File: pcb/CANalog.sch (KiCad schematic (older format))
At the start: 97 parts, among them J1 PWR, J2 USB_B_Micro, J3 SPI3, J4 I2C2, J5 STM_PROG, J6 ESP_PROG, J7 AOUT, J8 CAN, Q1 DMP3099L-7, Q2 MMBT2222A, Q3 DMP3099L-7, SW1 RESET, SW2 ESP_PROG, U1 BL9342, U2 RS321BXF, U3 STM32F302C8T6, U4 ESP-12F, U5 MIC5504-3.3YM5, U6 OPA330xxDBV, U7 SN65HVD230, U8 74AHC1G66, Y1 16MHz

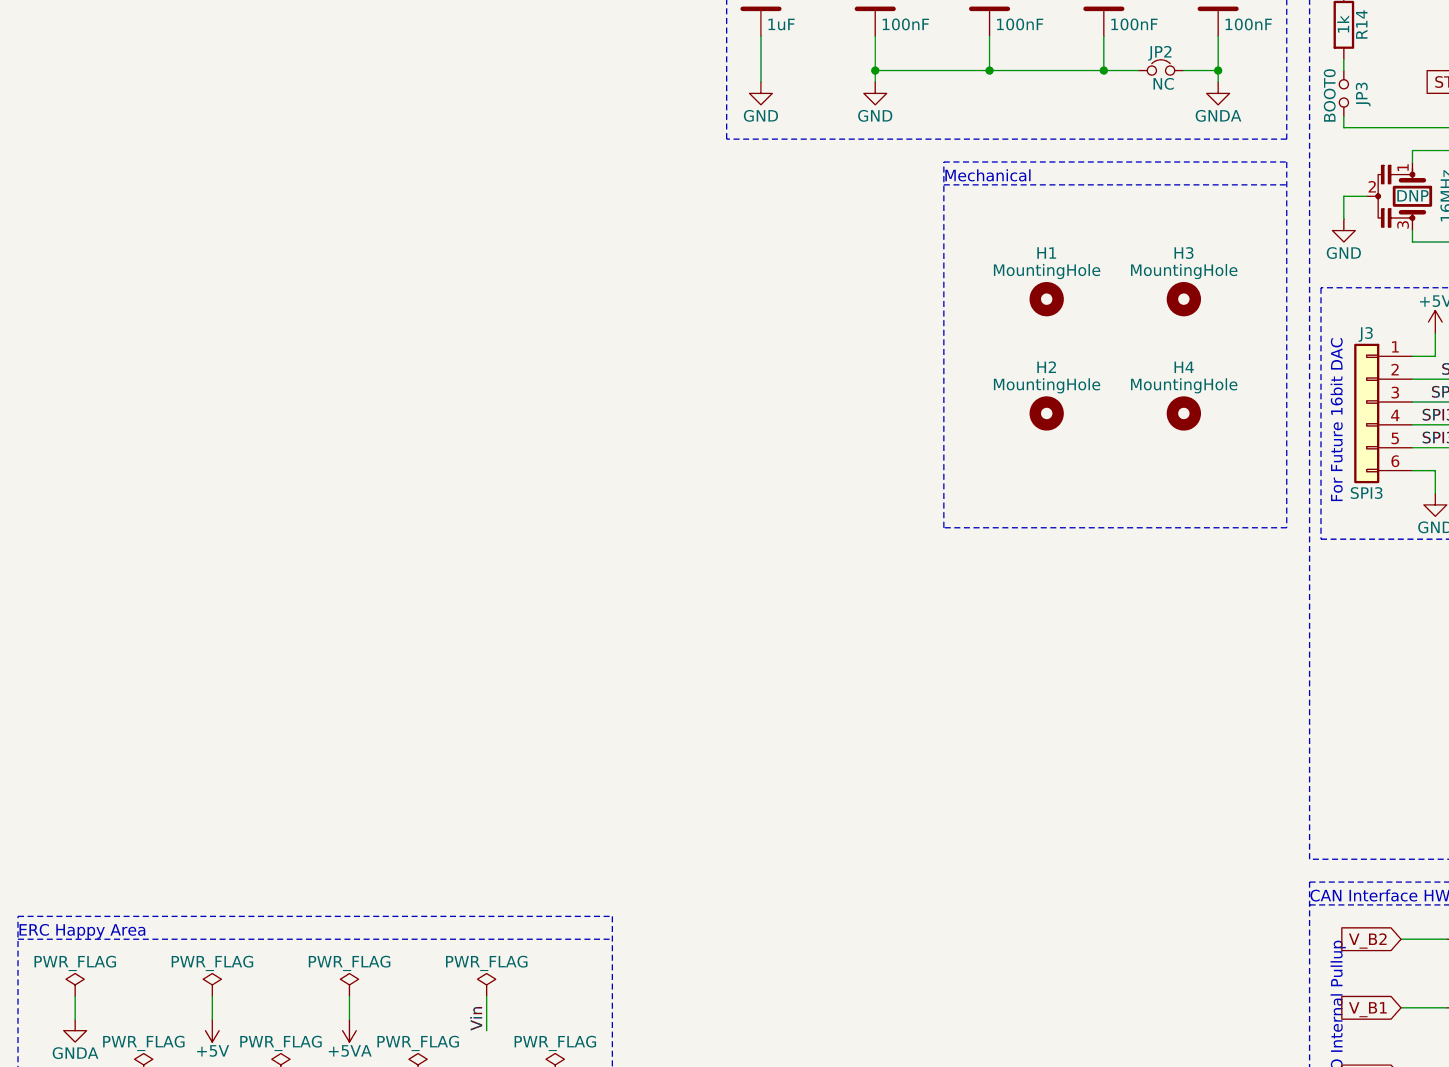
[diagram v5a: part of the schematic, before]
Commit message: usb fuse part number change to instock
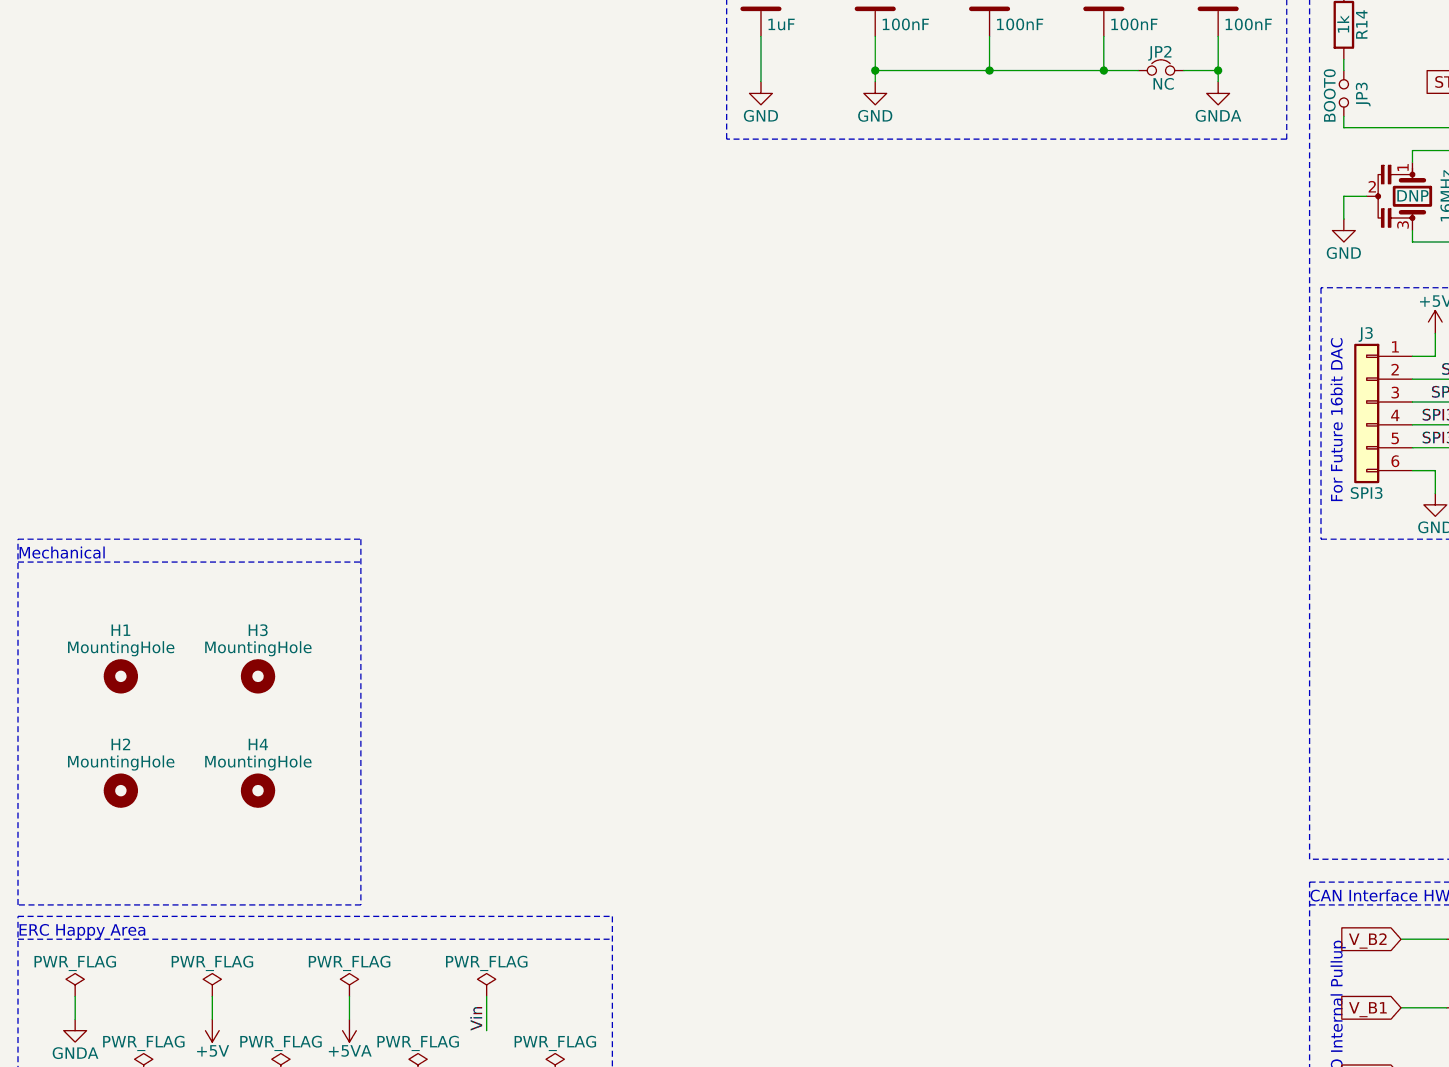
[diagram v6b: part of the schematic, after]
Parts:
- F1: MPN MF-FSMF050X-2 -> BSMD0603-050-6V; Manufacture Bourns -> BHFUSE; SPN C210357 -> C883095; Supplier Link https://lcsc.com/product-detail/Surface-Mount-Fuses_BOURNS_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 -> https://lcsc.com/product-detail/PTC-Resettable-Fuses_BHFUSE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
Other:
- moved on the sheet: H1, H2, H3, H4
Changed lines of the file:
@@
 L Mechanical:MountingHole H1
 U 1 1 61BCE530
-P 5050 6650
-F 0 "H1" H 5050 6850 50  0000 C CNN
-F 1 "MountingHole" H 5050 6775 50  0000 C CNN
-F 2 "MountingHole:MountingHole_2.7mm_M2.5" H 5050 6650 50  0001 C CNN
-F 3 "~" H 5050 6650 50  0001 C CNN
-	1    5050 6650
+P 1000 8300
+F 0 "H1" H 1000 8500 50  0000 C CNN
+F 1 "MountingHole" H 1000 8425 50  0000 C CNN
+F 2 "MountingHole:MountingHole_2.7mm_M2.5" H 1000 8300 50  0001 C CNN
+F 3 "~" H 1000 8300 50  0001 C CNN
+	1    1000 8300
 	1    0    0    -1
 $EndComp
@@
 L Mechanical:MountingHole H3
 U 1 1 61BCEAAF
-P 5650 6650
-F 0 "H3" H 5650 6850 50  0000 C CNN
-F 1 "MountingHole" H 5650 6775 50  0000 C CNN
-F 2 "MountingHole:MountingHole_2.7mm_M2.5" H 5650 6650 50  0001 C CNN
-F 3 "~" H 5650 6650 50  0001 C CNN
-	1    5650 6650
+P 1600 8300
+F 0 "H3" H 1600 8500 50  0000 C CNN
+F 1 "MountingHole" H 1600 8425 50  0000 C CNN
+F 2 "MountingHole:MountingHole_2.7mm_M2.5" H 1600 8300 50  0001 C CNN
+F 3 "~" H 1600 8300 50  0001 C CNN
+	1    1600 8300
 	1    0    0    -1
 $EndComp
@@
 L Mechanical:MountingHole H4
 U 1 1 61BCF017
-P 5650 7150
-F 0 "H4" H 5650 7350 50  0000 C CNN
-F 1 "MountingHole" H 5650 7275 50  0000 C CNN
-F 2 "MountingHole:MountingHole_2.7mm_M2.5" H 5650 7150 50  0001 C CNN
-F 3 "~" H 5650 7150 50  0001 C CNN
-	1    5650 7150
+P 1600 8800
+F 0 "H4" H 1600 9000 50  0000 C CNN
+F 1 "MountingHole" H 1600 8925 50  0000 C CNN
+F 2 "MountingHole:MountingHole_2.7mm_M2.5" H 1600 8800 50  0001 C CNN
+F 3 "~" H 1600 8800 50  0001 C CNN
+	1    1600 8800
 	1    0    0    -1
 $EndComp
@@
 L Mechanical:MountingHole H2
 U 1 1 61BCF67B
-P 5050 7150
-F 0 "H2" H 5050 7350 50  0000 C CNN
-F 1 "MountingHole" H 5050 7275 50  0000 C CNN
-F 2 "MountingHole:MountingHole_2.7mm_M2.5" H 5050 7150 50  0001 C CNN
-F 3 "~" H 5050 7150 50  0001 C CNN
-	1    5050 7150
+P 1000 8800
+F 0 "H2" H 1000 9000 50  0000 C CNN
+F 1 "MountingHole" H 1000 8925 50  0000 C CNN
+F 2 "MountingHole:MountingHole_2.7mm_M2.5" H 1000 8800 50  0001 C CNN
+F 3 "~" H 1000 8800 50  0001 C CNN
+	1    1000 8800
 	1    0    0    -1
 $EndComp
@@
 F 1 "500mA" V 1316 3050 50  0000 C CNN
 F 2 "Fuse:Fuse_0603_1608Metric_Castellated" H 1500 2850 50  0001 L CNN
-F 3 "~https://datasheet.lcsc.com/szlcsc/1806111858_BOURNS-MF-FSMF050X-2_C210357.pdf" H 1450 3050 50  0001 C CNN
-F 4 "MF-FSMF050X-2" H 1450 3050 50  0001 C CNN "MPN"
-F 5 "Bourns" H 1450 3050 50  0001 C CNN "Manufacture"
-F 6 "C210357" H 1450 3050 50  0001 C CNN "SPN"
+F 3 "https://datasheet.lcsc.com/szlcsc/2103231635_BHFUSE-BSMD0603-050-6V_C883095.pdf" H 1450 3050 50  0001 C CNN
+F 4 "BSMD0603-050-6V" H 1450 3050 50  0001 C CNN "MPN"
+F 5 " BHFUSE" H 1450 3050 50  0001 C CNN "Manufacture"
+F 6 "C883095" H 1450 3050 50  0001 C CNN "SPN"
 F 7 "LCSC" H 1450 3050 50  0001 C CNN "Supplier"
-F 8 "https://lcsc.com/product-detail/Surface-Mount-Fuses_BOURNS_MF-FSMF050X-2_BOURNS-MF-FSMF050X-2_C210357.html" H 1450 3050 50  0001 C CNN "Supplier Link"
+F 8 "https://lcsc.com/product-detail/PTC-Resettable-Fuses_BHFUSE-BSMD0603-050-6V_C883095.html" H 1450 3050 50  0001 C CNN "Supplier Link"
 	1    1450 3050
 	0    1    1    0
@@
 Text Notes 3900 3150 0    50   ~ 0
 Reset Circuitry
-Text Notes 4600 6150 0    50   ~ 0
+Text Notes 550  7800 0    50   ~ 0
 Mechanical
 Wire Notes Line
-	4600 6150 6100 6150
-Wire Notes Line
-	6100 7650 4600 7650
-Wire Notes Line
-	4600 7650 4600 6050
-Wire Notes Line
-	4600 6050 6100 6050
-Wire Notes Line
-	6100 6050 6100 7650
+	550  7800 2050 7800
+Wire Notes Line
+	2050 9300 550  9300
+Wire Notes Line
+	550  9300 550  7700
+Wire Notes Line
+	550  7700 2050 7700
+Wire Notes Line
+	2050 7700 2050 9300
 Text Notes 550  9450 0    50   ~ 0
 ERC Happy Area

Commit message: update ferrite with instock partnumber
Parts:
- FB1, FB2: MPN CBG160808U070T -> FCM1608KF-600T07; Manufacture FH(Guangdong Fenghua Advanced Tech) -> TAI-TECH; SPN C98494 -> C133931; Supplier Link https://lcsc.com/product-detail/Ferrite-Beads_FH-Guangdong-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 -> https://lcsc.com/product-detail/Ferrite-Beads_TAI-TECH-FCM1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
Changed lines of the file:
@@
 F 1 "FBS" V 12150 7350 50  0000 C CNN
 F 2 "Inductor_SMD:L_0603_1608Metric" V 11980 7350 50  0001 C CNN
-F 3 "https://datasheet.lcsc.com/szlcsc/2006221432_FH-Guangdong-Fenghua-Advanced-Tech-CBG160808U070T_C98494.pdf" H 12050 7350 50  0001 C CNN
-F 4 "CBG160808U070T" H 12050 7350 50  0001 C CNN "MPN"
-F 5 " FH(Guangdong Fenghua Advanced Tech)" H 12050 7350 50  0001 C CNN "Manufacture"
-F 6 "C98494" H 12050 7350 50  0001 C CNN "SPN"
+F 3 "https://datasheet.lcsc.com/szlcsc/2009171304_TAI-TECH-FCM1608KF-600T07_C133931.pdf" H 12050 7350 50  0001 C CNN
+F 4 "FCM1608KF-600T07" H 12050 7350 50  0001 C CNN "MPN"
+F 5 "TAI-TECH" H 12050 7350 50  0001 C CNN "Manufacture"
+F 6 "C133931" H 12050 7350 50  0001 C CNN "SPN"
 F 7 "LCSC" H 12050 7350 50  0001 C CNN "Supplier"
-F 8 "https://lcsc.com/product-detail/Ferrite-Beads_FH-Guangdong-Fenghua-Advanced-Tech-CBG160808U070T_C98494.html" H 12050 7350 50  0001 C CNN "Supplier Link"
+F 8 "https://lcsc.com/product-detail/Ferrite-Beads_TAI-TECH-FCM1608KF-600T07_C133931.html" H 12050 7350 50  0001 C CNN "Supplier Link"
 	1    12050 7350
 	0    -1   -1   0
@@
 F 1 "FBS" V 5650 5100 50  0000 C CNN
 F 2 "Inductor_SMD:L_0603_1608Metric" V 5480 5100 50  0001 C CNN
-F 3 "https://datasheet.lcsc.com/szlcsc/2006221432_FH-Guangdong-Fenghua-Advanced-Tech-CBG160808U070T_C98494.pdf" H 5550 5100 50  0001 C CNN
-F 4 "CBG160808U070T" H 5550 5100 50  0001 C CNN "MPN"
-F 5 " FH(Guangdong Fenghua Advanced Tech)" H 5550 5100 50  0001 C CNN "Manufacture"
-F 6 "C98494" H 5550 5100 50  0001 C CNN "SPN"
+F 3 "https://datasheet.lcsc.com/szlcsc/2009171304_TAI-TECH-FCM1608KF-600T07_C133931.pdf" H 5550 5100 50  0001 C CNN
+F 4 "FCM1608KF-600T07" H 5550 5100 50  0001 C CNN "MPN"
+F 5 "TAI-TECH" H 5550 5100 50  0001 C CNN "Manufacture"
+F 6 "C133931" H 5550 5100 50  0001 C CNN "SPN"
 F 7 "LCSC" H 5550 5100 50  0001 C CNN "Supplier"
-F 8 "https://lcsc.com/product-detail/Ferrite-Beads_FH-Guangdong-Fenghua-Advanced-Tech-CBG160808U070T_C98494.html" H 5550 5100 50  0001 C CNN "Supplier Link"
+F 8 "https://lcsc.com/product-detail/Ferrite-Beads_TAI-TECH-FCM1608KF-600T07_C133931.html" H 5550 5100 50  0001 C CNN "Supplier Link"
 	1    5550 5100
 	0    -1   -1   0

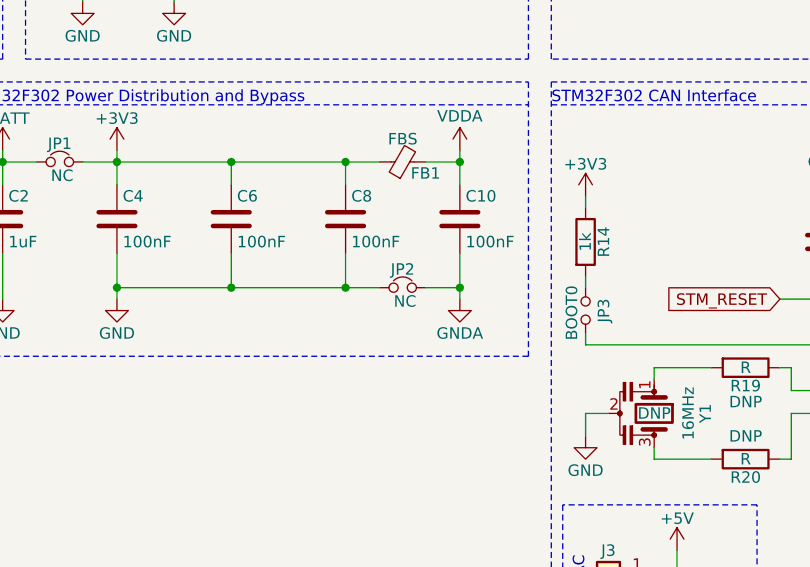
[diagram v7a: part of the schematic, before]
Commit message: replace agnd jumper to gnd with net tie
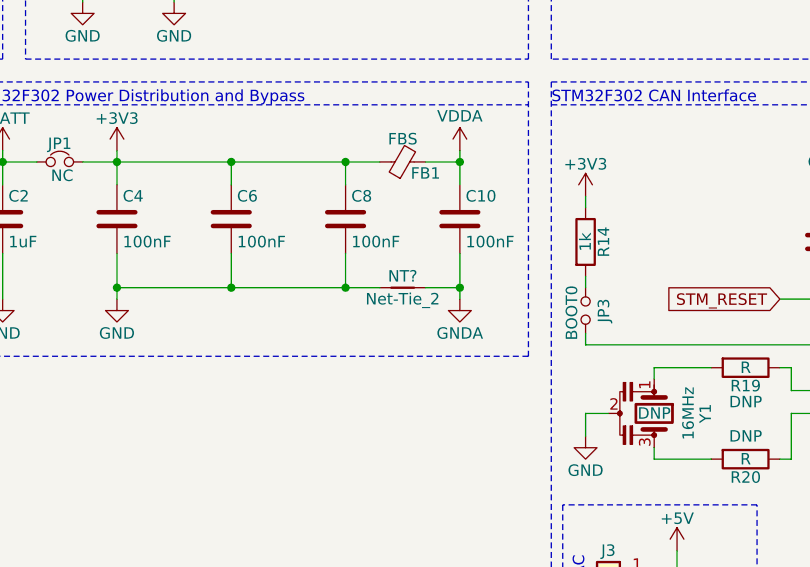
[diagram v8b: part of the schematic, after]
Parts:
- removed JP2: NC, Jumper:SolderJumper-2_P1.3mm_Bridged_RoundedPad1.0x1.5mm, symbol Device:Jumper_NC_Small
- added NT?: Net-Tie_2, NetTie:NetTie-2_SMD_Pad0.5mm, symbol Device:Net-Tie_2
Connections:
- net GND: now also NT?.1
- net GNDA: now also NT?.2
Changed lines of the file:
@@
 Wire Wire Line
 	5800 5050 5800 5100
-Wire Wire Line
-	5800 5700 5800 5650
 $Comp
 L Device:C C10
@@
 	1    0    0    -1
 $EndComp
-$Comp
-L Device:Jumper_NC_Small JP2
-U 1 1 619EAE49
-P 5550 5650
-F 0 "JP2" H 5550 5730 50  0000 C CNN
-F 1 "NC" H 5560 5590 50  0000 C CNN
-F 2 "Jumper:SolderJumper-2_P1.3mm_Bridged_RoundedPad1.0x1.5mm" H 5550 5650 50  0001 C CNN
-F 3 "~" H 5550 5650 50  0001 C CNN
-F 4 "DNP" H 5550 5650 50  0001 C CNN "Population"
-	1    5550 5650
-	1    0    0    -1
-$EndComp
-Wire Wire Line
-	5650 5650 5800 5650
-Connection ~ 5800 5650
-Wire Wire Line
-	5800 5650 5800 5500
-Wire Wire Line
-	5450 5650 5300 5650
-Connection ~ 5300 5650
 $Comp
 L Mechanical:MountingHole H1
@@
 Text Notes 3200 2250 1    50   ~ 0
 EN Pin Vmax = 5V
+$Comp
+L Device:Net-Tie_2 NT?
+U 1 1 606F5FFD
+P 5550 5650
+F 0 "NT?" H 5550 5700 50  0000 C CNN
+F 1 "Net-Tie_2" H 5550 5600 50  0000 C CNN
+F 2 "NetTie:NetTie-2_SMD_Pad0.5mm" H 5550 5650 50  0001 C CNN
+F 3 "~" H 5550 5650 50  0001 C CNN
+	1    5550 5650
+	1    0    0    -1
+$EndComp
+Wire Wire Line
+	5800 5500 5800 5650
+Wire Wire Line
+	5450 5650 5300 5650
+Connection ~ 5300 5650
+Wire Wire Line
+	5650 5650 5800 5650
+Connection ~ 5800 5650
+Wire Wire Line
+	5800 5650 5800 5700
 $EndSCHEMATC
